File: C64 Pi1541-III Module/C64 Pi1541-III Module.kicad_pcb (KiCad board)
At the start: 2 copper layers, 100 x 100 mm, 21 parts, among them J1 DC IN, J2 C64_IEC, J3 C64_IEC, J8 Module_Panel, M1 Mounting, M2 Mounting, M3 Mounting, M4 Mounting, U1 7406

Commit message: First layout done
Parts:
- added R3: 10k, resistor:R_Axial_DIN0207_L6.3mm_D2.5mm_P10.16mm_Horizontal, F.Cu at (132.1, 81.9)
- added R4: 10k, resistor:R_Axial_DIN0207_L6.3mm_D2.5mm_P10.16mm_Horizontal, F.Cu at (132.1, 78.1)
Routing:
- net +3V3: track 187.0 -> 214.6 mm
- net SW3_DOWN: track 83.9 -> 94.0 mm
- net SW2_UP: track 78.3 -> 86.7 mm

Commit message: Fix DIN-footprint
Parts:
- added G***: LOGO, pi1541:Pi1541-logo3, F.Cu at (102.2, 97.2)
- added Pi1541-drive: , pi1541:Pi1541-drive, F.Cu at (115.6, 118.7)
- moved REF*** 12.1 mm to (149.9, 127.6)
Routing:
- net C64_DATA: track 146.6 -> 155.2 mm
- net C64_CLK: track 125.8 -> 132.9 mm, vias 1 -> 2
- net C64_ATN: track 67.5 -> 64.4 mm, vias 2 -> 0
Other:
- board text added: "Module (rev. B)"
- board text removed: "PI1541-III Module (rev. A) github.com/tebl"

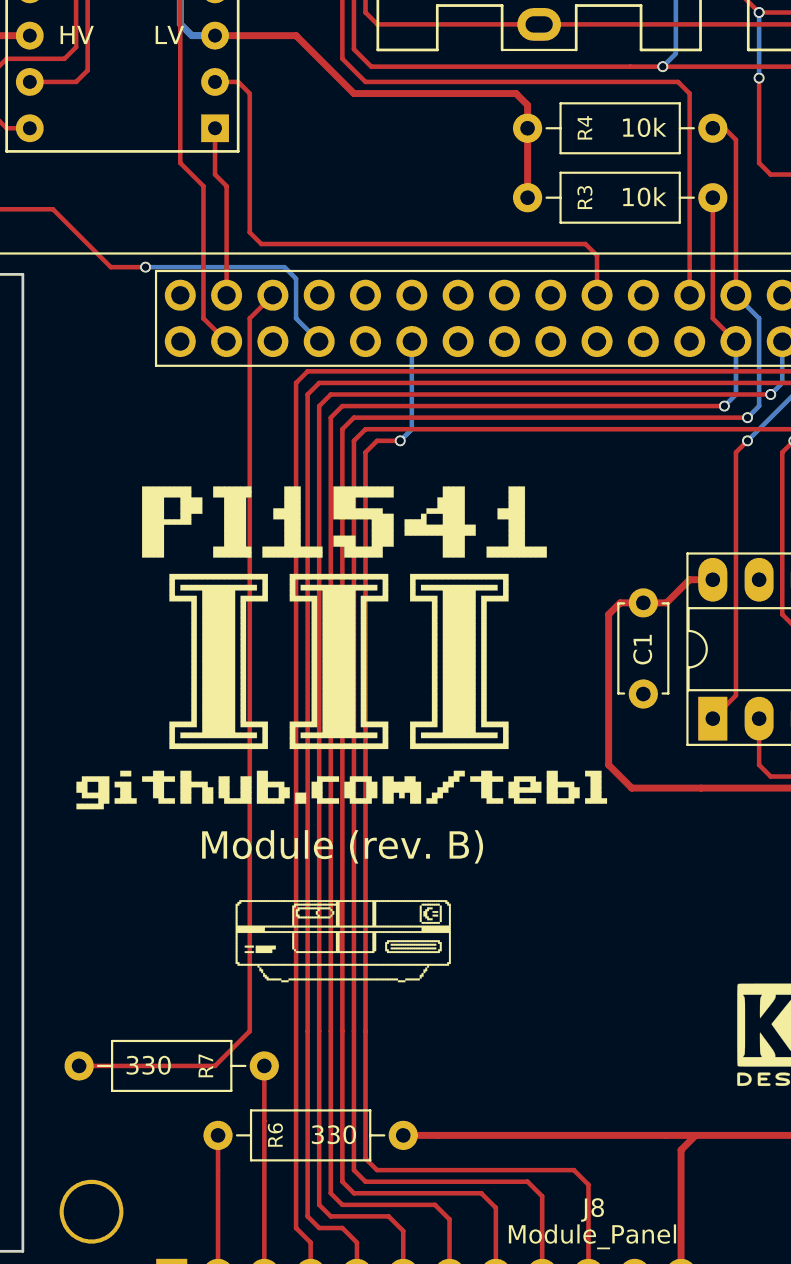
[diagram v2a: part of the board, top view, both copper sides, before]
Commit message: Adjust LED resistor value
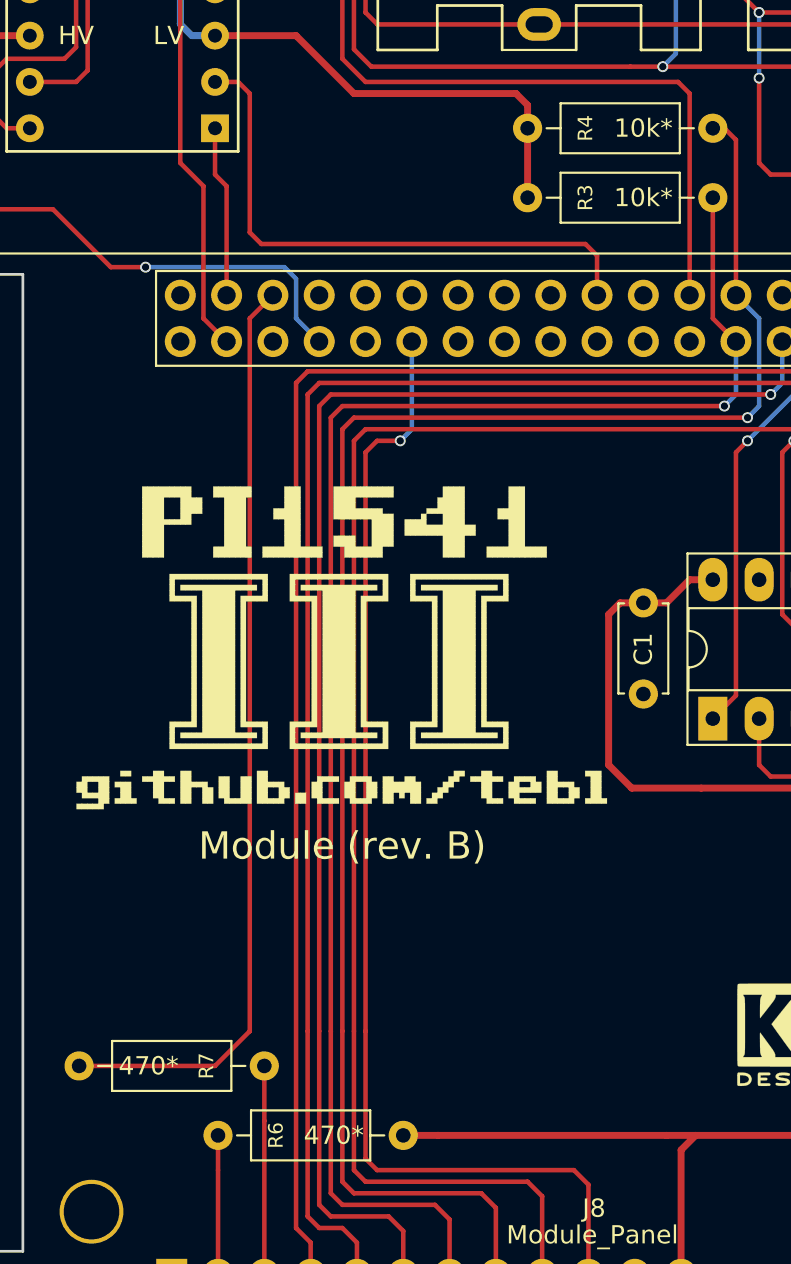
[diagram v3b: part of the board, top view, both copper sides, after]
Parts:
- Pi1541-drive: moved to B.Cu
- R3, R4: value 10k -> 10k*
- R6, R7: value 330 -> 470*
- moved Pi1541-drive 75.5 mm to (159.4, 57.3), turned to 180 degrees

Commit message: Exported files
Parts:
- A1: value Raspberry PI -> Raspberry PI 3A/3B
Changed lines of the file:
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@@
       (effects (font (size 1 1) (thickness 0.15)))
     )
-    (fp_text value "Raspberry PI" (at -5.985 66.04 180) (layer F.SilkS)
+    (fp_text value "Raspberry PI 3A/3B" (at -5.985 62.865 180) (layer F.SilkS)
       (effects (font (size 1 1) (thickness 0.15)))
     )
